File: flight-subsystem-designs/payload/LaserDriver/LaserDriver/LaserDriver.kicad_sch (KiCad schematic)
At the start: 28 parts, among them J1 Conn_Coaxial, J2 Laser 0, J3 Laser 1, J5 VIN, U1 74LVC1G04, U2 SY100ELT22ZG-TR, U3 MAX3967AETG+, U4 MAX3967AETG+, U5 NCV8161AMX330TBG

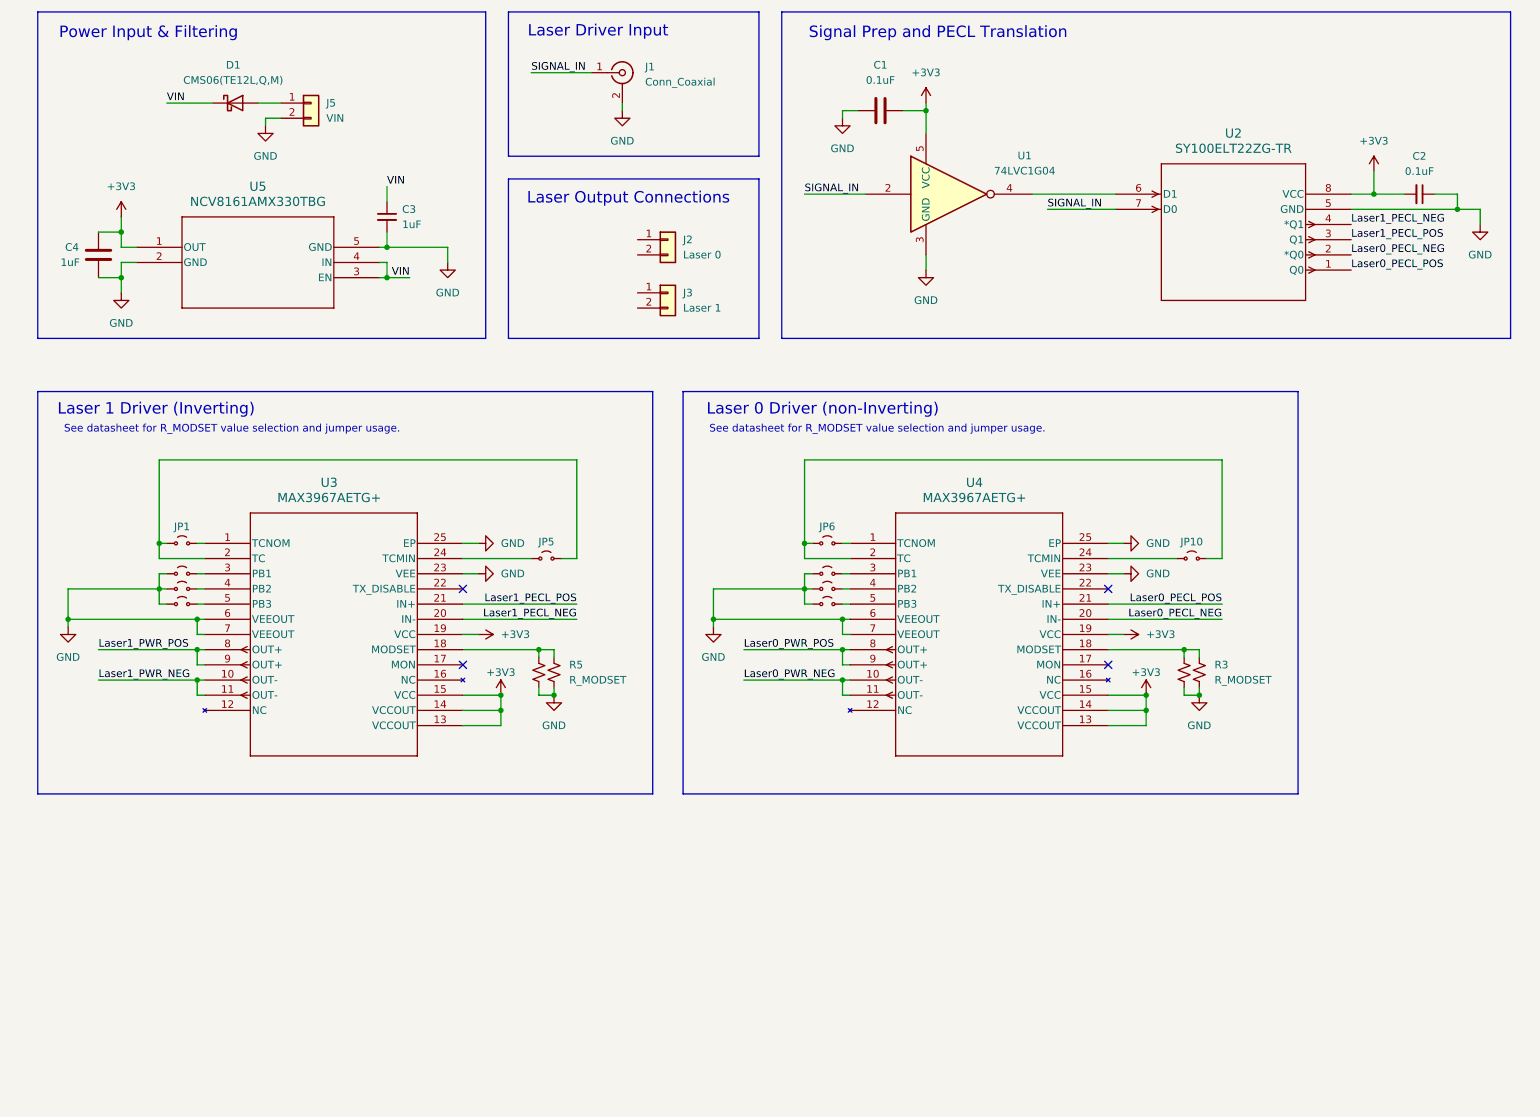
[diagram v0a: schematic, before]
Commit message: laserdriver: add terminations and some fixups
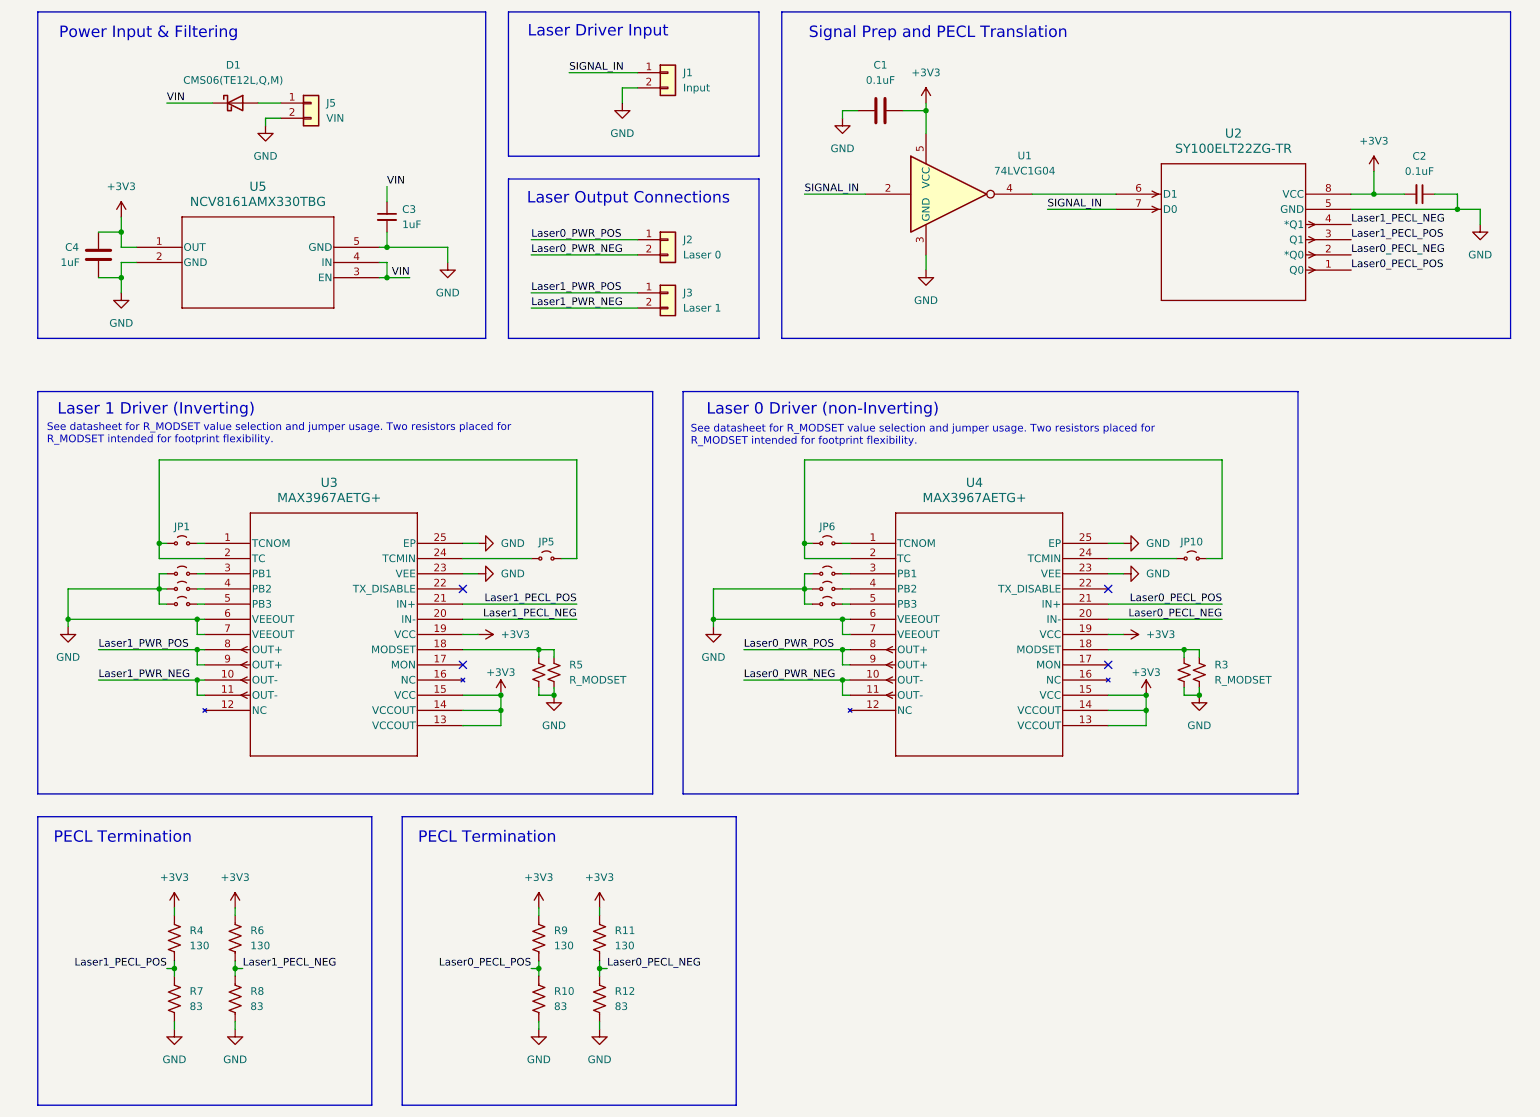
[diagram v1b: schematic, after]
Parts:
- removed J1: Conn_Coaxial, symbol Connector:Conn_Coaxial
- added J1: Input, symbol Connector_Generic:Conn_01x02
- added R10, R12, R7, R8: 83, symbol Device:R_US
- added R11, R4, R6, R9: 130, symbol Device:R_US
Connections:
- net +3V3: now also R11.1, R4.1, R6.1, R9.1
- net GND: now also J1.2 (Pin_2), R10.2, R12.2, R7.2, R8.2
- net Laser0_PECL_NEG: now also R11.2, R12.1
- net Laser0_PECL_POS: now also R10.1, R9.2
- net Laser0_PWR_NEG: now also J2.2 (Pin_2)
- net Laser0_PWR_POS: now also J2.1 (Pin_1)
- net Laser1_PECL_NEG: now also R6.2, R8.1
- net Laser1_PECL_POS: now also R4.2, R7.1
- net Laser1_PWR_NEG: now also J3.2 (Pin_2)
- net Laser1_PWR_POS: now also J3.1 (Pin_1)
- net SIGNAL_IN: now also J1.1 (Pin_1)
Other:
- note added: "PECL Termination"
- note added: "See datasheet for R_MODSET value selection and jumper usage. Two resistors placed for R_MODSET intended for footprint flexibility."
- note removed: "See datasheet for R_MODSET value selection and jumper usage."

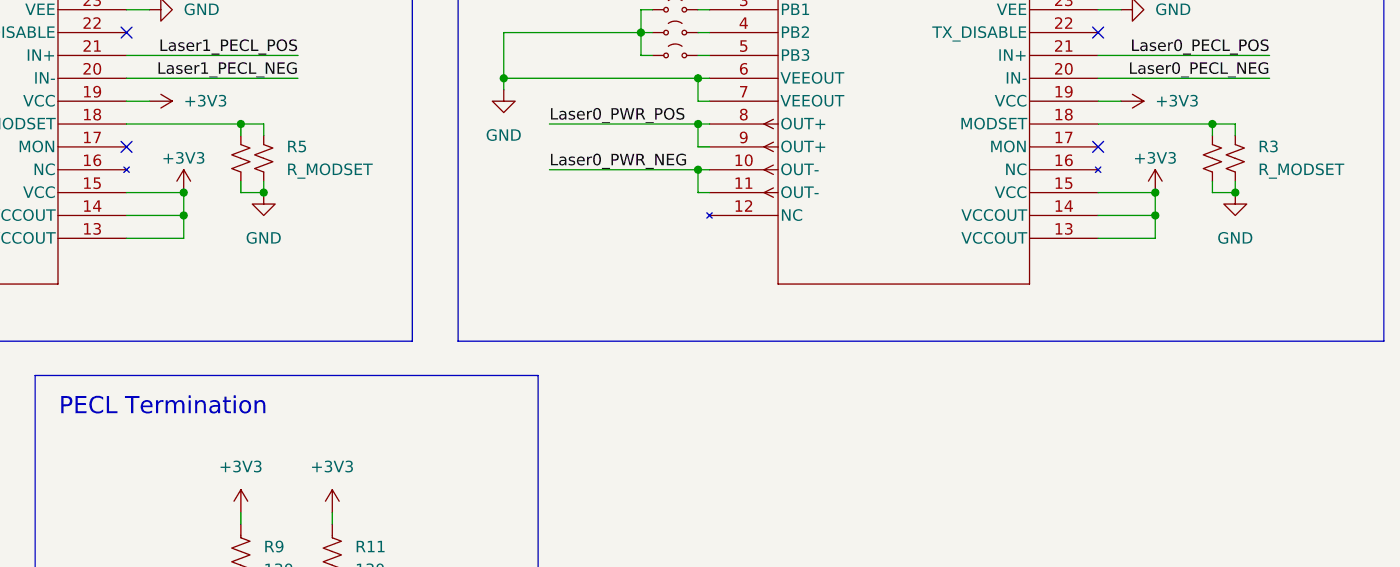
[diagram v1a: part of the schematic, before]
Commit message: laserdriver: forgot my decouplign caps
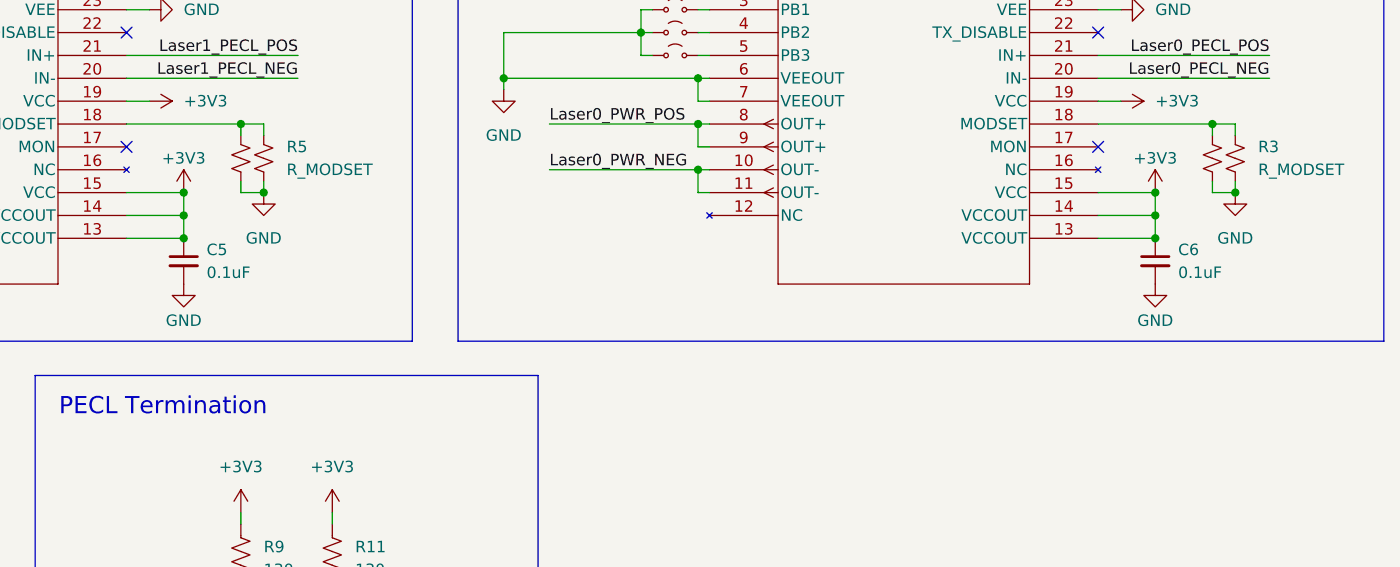
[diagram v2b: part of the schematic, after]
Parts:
- added C5, C6: 0.1uF, symbol Device:C_Small
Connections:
- net +3V3: now also C5.1, C6.1
- net GND: now also C5.2, C6.2

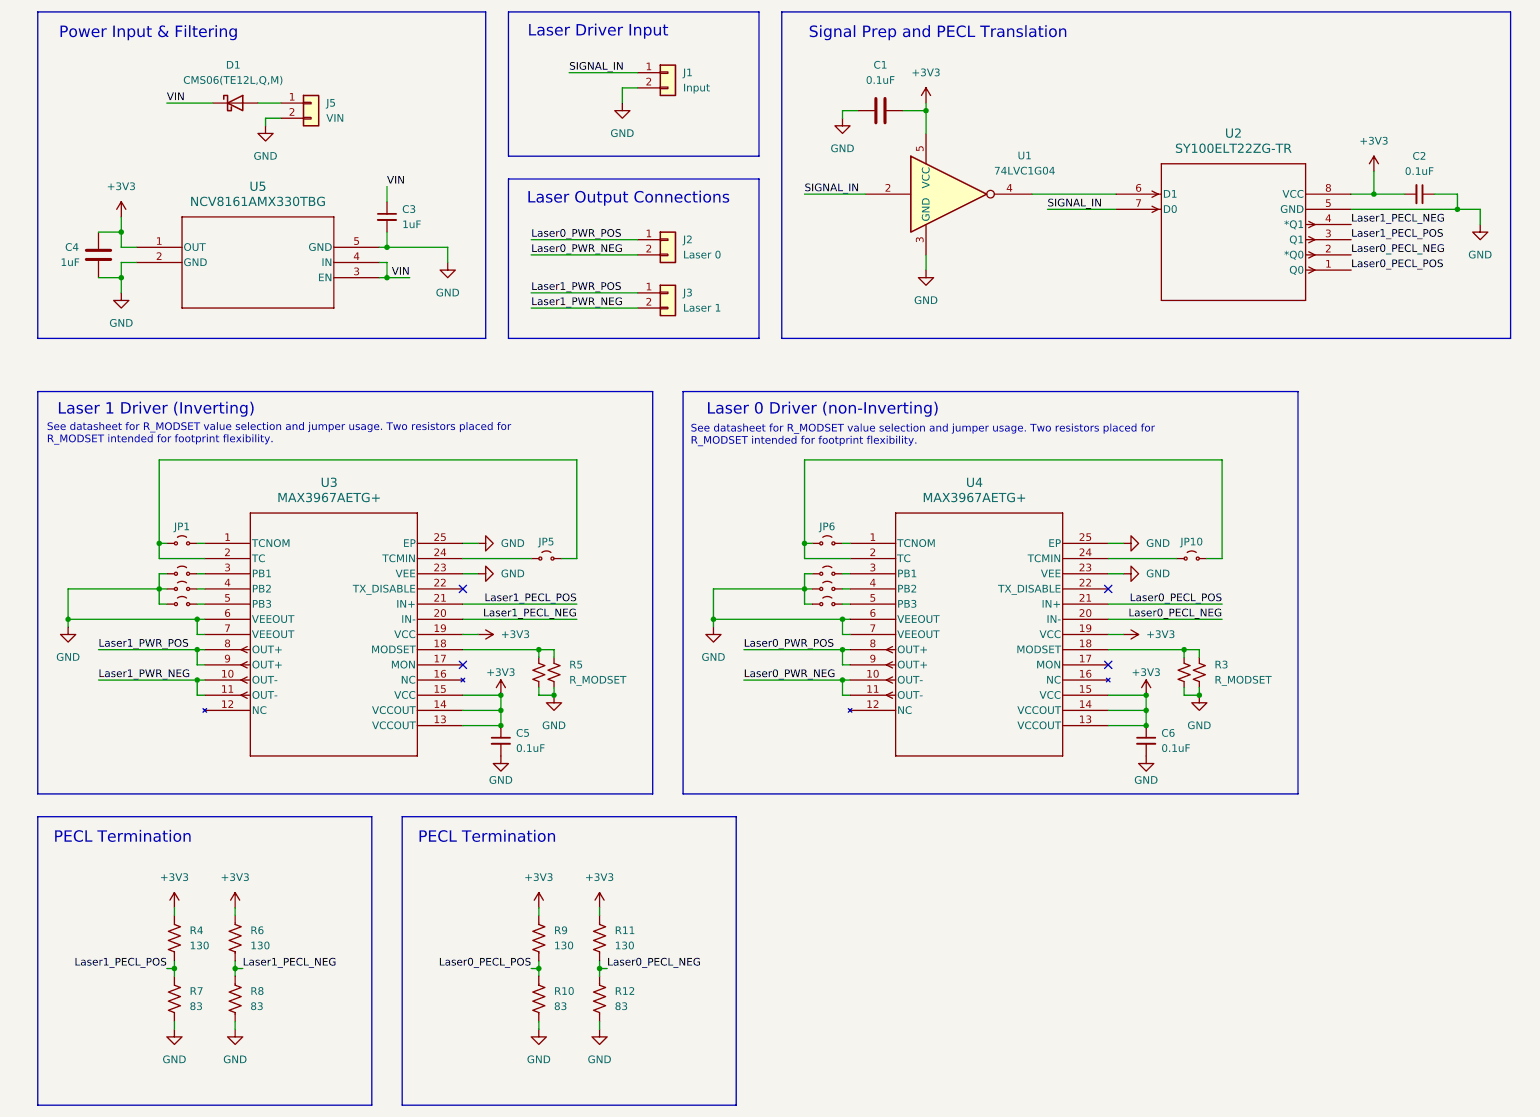
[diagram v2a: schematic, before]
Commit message: laserdriver: add ferrite beads and assign footprints
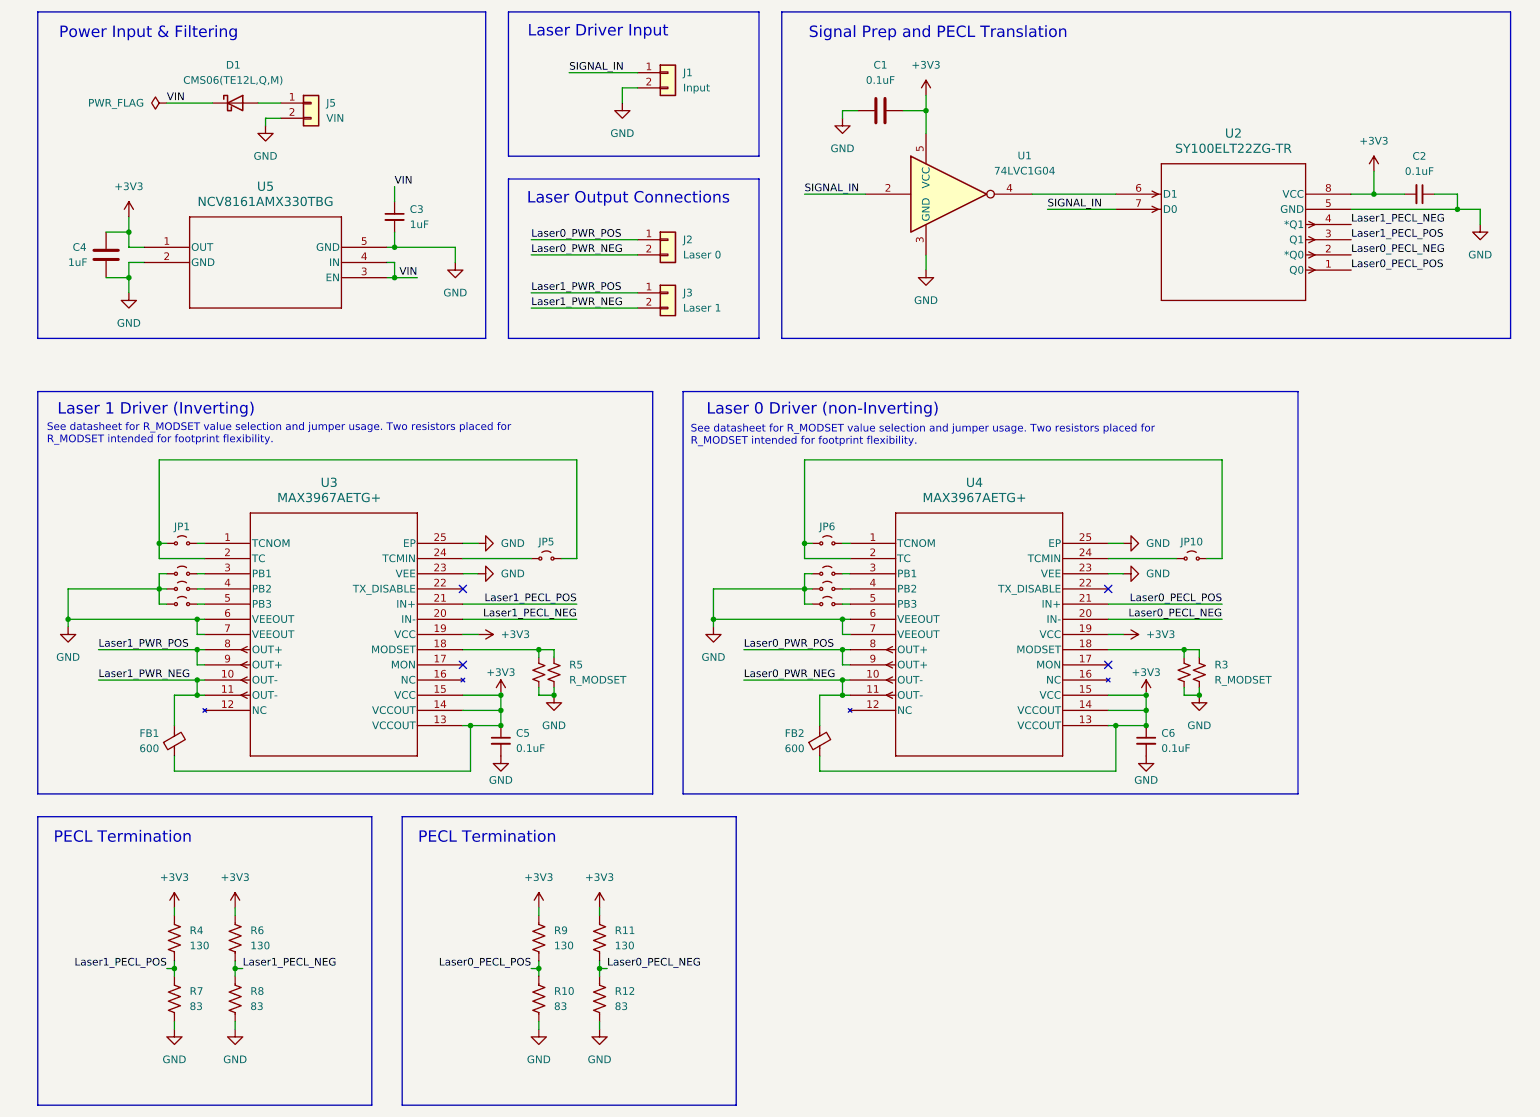
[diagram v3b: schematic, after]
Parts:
- added FB1, FB2: 600, Inductor_SMD:L_0805_2012Metric_Pad1.05x1.20mm_HandSolder, symbol Device:FerriteBead_Small
- C1, C2, C3, C4, C5, C6: footprint (none) -> Capacitor_SMD:C_0805_2012Metric_Pad1.18x1.45mm_HandSolder
- J1, J2, J3, J5: footprint (none) -> Connector_PinHeader_2.54mm:PinHeader_1x02_P2.54mm_Vertical
- R10, R11, R12, R4, R6, R7, R8, R9, U1: footprint (none) -> Resistor_SMD:R_0805_2012Metric_Pad1.20x1.40mm_HandSolder
- U2: footprint SOIC-8_M_MCH -> footprints:SOIC-8_M_MCH
- U3, U4: footprint 21-0139_T2444+4_MXM -> footprints:21-0139_T2444&plus_4_MXM
- U5: footprint XDFN4_711AJ_OSI -> footprints:XDFN4_711AJ_OSI
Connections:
- net +3V3: now also FB1.1, FB2.1
- net Laser0_PWR_NEG: now also FB2.2
- net Laser1_PWR_NEG: now also FB1.2
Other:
- moved on the sheet: C3, C4, U5
